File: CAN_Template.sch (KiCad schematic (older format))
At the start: 18 parts

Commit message: Added stack connector and populated PCB
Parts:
- gave numbers to parts that had none: 18
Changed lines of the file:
@@
 EESchema Schematic File Version 4
+LIBS:MASA-Radio Board-cache
 EELAYER 30 0
 EELAYER END
@@
 $EndDescr
 $Comp
-L Device:R_US NP?
+L Device:R_US NP1
 U 1 1 5DCB3E43
 P 6600 3250
-F 0 "NP?" H 6668 3296 50  0000 L CNN
+F 0 "NP1" H 6668 3296 50  0000 L CNN
 F 1 "60" H 6668 3205 50  0000 L CNN
 F 2 "Resistor_SMD:R_0805_2012Metric_Pad1.15x1.40mm_HandSolder" V 6640 3240 50  0001 C CNN
@@
 $EndComp
 $Comp
-L Device:C C?
+L Device:C C3
 U 1 1 5DCB7D7B
 P 4300 2950
-F 0 "C?" V 4048 2950 50  0000 C CNN
+F 0 "C3" V 4048 2950 50  0000 C CNN
 F 1 "100pf" V 4139 2950 50  0000 C CNN
 F 2 "Capacitor_SMD:C_0805_2012Metric_Pad1.15x1.40mm_HandSolder" H 4338 2800 50  0001 C CNN
@@
 $EndComp
 $Comp
-L Device:C C?
+L Device:C C5
 U 1 1 5DCB9CD1
 P 5750 2700
-F 0 "C?" V 5498 2700 50  0000 C CNN
+F 0 "C5" V 5498 2700 50  0000 C CNN
 F 1 "1nf" V 5589 2700 50  0000 C CNN
 F 2 "Capacitor_SMD:C_0805_2012Metric_Pad1.15x1.40mm_HandSolder" H 5788 2550 50  0001 C CNN
@@
 $EndComp
 $Comp
-L Device:C C?
+L Device:C C12
 U 1 1 5DCBAD85
 P 5750 2900
-F 0 "C?" V 5650 2700 50  0000 C CNN
+F 0 "C12" V 5650 2700 50  0000 C CNN
 F 1 "100nf" V 5589 2900 50  0000 C CNN
 F 2 "Capacitor_SMD:C_0805_2012Metric_Pad1.15x1.40mm_HandSolder" H 5788 2750 50  0001 C CNN
@@
 $EndComp
 $Comp
-L power:GND #PWR?
+L power:GND #PWR031
 U 1 1 5DCE500D
 P 3500 3050
-F 0 "#PWR?" H 3500 2800 50  0001 C CNN
+F 0 "#PWR031" H 3500 2800 50  0001 C CNN
 F 1 "GND" H 3505 2877 50  0000 C CNN
 F 2 "" H 3500 3050 50  0001 C CNN
@@
 $EndComp
 $Comp
-L Device:C C?
+L Device:C C14
 U 1 1 5DCE6703
 P 6600 4150
-F 0 "C?" H 6715 4196 50  0000 L CNN
+F 0 "C14" H 6715 4196 50  0000 L CNN
 F 1 "100pf" H 6715 4105 50  0000 L CNN
 F 2 "Capacitor_SMD:C_0805_2012Metric_Pad1.15x1.40mm_HandSolder" H 6638 4000 50  0001 C CNN
@@
 $EndComp
 $Comp
-L Device:R_US NP?
+L Device:R_US NP2
 U 1 1 5DCE98D1
 P 6600 3650
-F 0 "NP?" H 6668 3696 50  0000 L CNN
+F 0 "NP2" H 6668 3696 50  0000 L CNN
 F 1 "60" H 6668 3605 50  0000 L CNN
 F 2 "Resistor_SMD:R_0805_2012Metric_Pad1.15x1.40mm_HandSolder" V 6640 3640 50  0001 C CNN
@@
 $EndComp
 $Comp
-L Device:C C?
+L Device:C C15
 U 1 1 5DCEFDFD
 P 6900 3450
-F 0 "C?" H 7015 3496 50  0000 L CNN
+F 0 "C15" H 7015 3496 50  0000 L CNN
 F 1 "1nf" H 7015 3405 50  0000 L CNN
 F 2 "Capacitor_SMD:C_0805_2012Metric_Pad1.15x1.40mm_HandSolder" H 6938 3300 50  0001 C CNN
@@
 $EndComp
 $Comp
-L power:GND #PWR?
+L power:GND #PWR041
 U 1 1 5DCF0F65
 P 6600 4300
-F 0 "#PWR?" H 6600 4050 50  0001 C CNN
+F 0 "#PWR041" H 6600 4050 50  0001 C CNN
 F 1 "GND" H 6605 4127 50  0000 C CNN
 F 2 "" H 6600 4300 50  0001 C CNN
@@
 $EndComp
 $Comp
-L power:GND #PWR?
+L power:GND #PWR040
 U 1 1 5DCF11EA
 P 6600 2600
-F 0 "#PWR?" H 6600 2350 50  0001 C CNN
+F 0 "#PWR040" H 6600 2350 50  0001 C CNN
 F 1 "GND" H 6605 2427 50  0000 C CNN
 F 2 "" H 6600 2600 50  0001 C CNN
@@
 $EndComp
 $Comp
-L Device:R_US R?
+L Device:R_US R4
 U 1 1 5DCF1CE0
 P 6300 3450
-F 0 "R?" H 6368 3496 50  0000 L CNN
+F 0 "R4" H 6368 3496 50  0000 L CNN
 F 1 "0" H 6368 3405 50  0000 L CNN
 F 2 "Resistor_SMD:R_0805_2012Metric_Pad1.15x1.40mm_HandSolder" V 6340 3440 50  0001 C CNN
@@
 $EndComp
 $Comp
-L Device:D_TVS_x2_CAA D?
+L Device:D_TVS_x2_CAA D2
 U 1 1 5DD0169A
 P 7350 3450
-F 0 "D?" V 7304 3529 50  0000 L CNN
+F 0 "D2" V 7304 3529 50  0000 L CNN
 F 1 "D5V0L2B3W-7" V 7395 3529 50  0000 L CNN
 F 2 "Package_TO_SOT_SMD:SOT-23" H 7200 3450 50  0001 C CNN
@@
 $EndComp
 $Comp
-L Device:R_US R?
+L Device:R_US R3
 U 1 1 5DD5BD7B
 P 4850 3900
-F 0 "R?" H 4918 3946 50  0000 L CNN
+F 0 "R3" H 4918 3946 50  0000 L CNN
 F 1 "10k" H 4918 3855 50  0000 L CNN
 F 2 "Resistor_SMD:R_0805_2012Metric_Pad1.15x1.40mm_HandSolder" V 4890 3890 50  0001 C CNN
@@
 $EndComp
 $Comp
-L Device:R_US R?
+L Device:R_US R2
 U 1 1 5DD67335
 P 4600 3350
-F 0 "R?" H 4668 3396 50  0000 L CNN
+F 0 "R2" H 4668 3396 50  0000 L CNN
 F 1 "0" H 4668 3305 50  0000 L CNN
 F 2 "Resistor_SMD:R_0805_2012Metric_Pad1.15x1.40mm_HandSolder" V 4640 3340 50  0001 C CNN
@@
 $EndComp
 $Comp
-L Interface_CAN_LIN:MCP2515-xSO U?
+L Interface_CAN_LIN:MCP2515-xSO U5
 U 1 1 5DCB05B0
 P 3500 3850
-F 0 "U?" H 3500 3950 50  0000 C CNN
+F 0 "U5" H 3500 3950 50  0000 C CNN
 F 1 "MCP2515-xSO" H 3500 4050 50  0000 C CNN
 F 2 "Package_SO:SOIC-18W_7.5x11.6mm_P1.27mm" H 3500 2950 50  0001 C CIN
@@
 CAN_H
 $Comp
-L Device:C C?
+L Device:C C13
 U 1 1 5DCE5998
 P 6600 2750
-F 0 "C?" H 6715 2796 50  0000 L CNN
+F 0 "C13" H 6715 2796 50  0000 L CNN
 F 1 "100pf" H 6715 2705 50  0000 L CNN
 F 2 "Capacitor_SMD:C_0805_2012Metric_Pad1.15x1.40mm_HandSolder" H 6638 2600 50  0001 C CNN
@@
 $EndComp
 $Comp
-L Interface_CAN_LIN:SN65HVD1050D U?
+L Interface_CAN_LIN:SN65HVD1050D U6
 U 1 1 5DD4ABBA
 P 5450 3450
-F 0 "U?" H 5350 3500 50  0000 C CNN
+F 0 "U6" H 5350 3500 50  0000 C CNN
 F 1 "SN65HVD1050D" H 5350 3400 50  0000 C CNN
 F 2 "Package_SO:SOIC-8_3.9x4.9mm_P1.27mm" H 5450 2950 50  0001 C CNN
@@
 Connection ~ 7350 3000
 $Comp
-L power:GND #PWR?
+L power:GND #PWR037
 U 1 1 5E09CBC9
 P 5450 3850
-F 0 "#PWR?" H 5450 3600 50  0001 C CNN
+F 0 "#PWR037" H 5450 3600 50  0001 C CNN
 F 1 "GND" H 5455 3677 50  0000 C CNN
 F 2 "" H 5450 3850 50  0001 C CNN
@@
 $EndComp
 $Comp
-L power:GND #PWR?
+L power:GND #PWR039
 U 1 1 5E0A1057
 P 5900 2900
-F 0 "#PWR?" H 5900 2650 50  0001 C CNN
+F 0 "#PWR039" H 5900 2650 50  0001 C CNN
 F 1 "GND" H 5905 2727 50  0000 C CNN
 F 2 "" H 5900 2900 50  0001 C CNN
@@
 $EndComp
 $Comp
-L power:GND #PWR?
+L power:GND #PWR038
 U 1 1 5E0A1679
 P 5900 2700
-F 0 "#PWR?" H 5900 2450 50  0001 C CNN
+F 0 "#PWR038" H 5900 2450 50  0001 C CNN
 F 1 "GND" H 5905 2527 50  0000 C CNN
 F 2 "" H 5900 2700 50  0001 C CNN
@@
 Connection ~ 5450 2900
 $Comp
-L power:+5V #PWR?
+L power:+5V #PWR036
 U 1 1 5E0A2EDD
 P 5450 2700
-F 0 "#PWR?" H 5450 2550 50  0001 C CNN
+F 0 "#PWR036" H 5450 2550 50  0001 C CNN
 F 1 "+5V" V 5465 2828 50  0000 L CNN
 F 2 "" H 5450 2700 50  0001 C CNN
@@
 	4850 3650 4950 3650
 $Comp
-L power:GND #PWR?
+L power:GND #PWR035
 U 1 1 5E0A7026
 P 4850 4050
-F 0 "#PWR?" H 4850 3800 50  0001 C CNN
+F 0 "#PWR035" H 4850 3800 50  0001 C CNN
 F 1 "GND" H 4855 3877 50  0000 C CNN
 F 2 "" H 4850 4050 50  0001 C CNN
@@
 $EndComp
 $Comp
-L Device:R_US R?
+L Device:R_US R1
 U 1 1 5E0A7D89
 P 4600 3250
-F 0 "R?" H 4668 3296 50  0000 L CNN
+F 0 "R1" H 4668 3296 50  0000 L CNN
 F 1 "0" H 4668 3205 50  0000 L CNN
 F 2 "Resistor_SMD:R_0805_2012Metric_Pad1.15x1.40mm_HandSolder" V 4640 3240 50  0001 C CNN
@@
 	4750 3350 4850 3350
 $Comp
-L power:GND #PWR?
+L power:GND #PWR033
 U 1 1 5E0B3A8E
 P 4300 2800
-F 0 "#PWR?" H 4300 2550 50  0001 C CNN
+F 0 "#PWR033" H 4300 2550 50  0001 C CNN
 F 1 "GND" H 4305 2627 50  0000 C CNN
 F 2 "" H 4300 2800 50  0001 C CNN
@@
 $EndComp
 $Comp
-L Device:C C?
+L Device:C C2
 U 1 1 5E0BDAE5
 P 3200 5000
-F 0 "C?" V 2948 5000 50  0000 C CNN
+F 0 "C2" V 2948 5000 50  0000 C CNN
 F 1 "1nf" V 3039 5000 50  0000 C CNN
 F 2 "Capacitor_SMD:C_0805_2012Metric_Pad1.15x1.40mm_HandSolder" H 3238 4850 50  0001 C CNN
@@
 $EndComp
 $Comp
-L Device:C C?
+L Device:C C1
 U 1 1 5E0BDAEB
 P 3200 4800
-F 0 "C?" V 3100 4600 50  0000 C CNN
+F 0 "C1" V 3100 4600 50  0000 C CNN
 F 1 "100nf" V 3039 4800 50  0000 C CNN
 F 2 "Capacitor_SMD:C_0805_2012Metric_Pad1.15x1.40mm_HandSolder" H 3238 4650 50  0001 C CNN
@@
 $EndComp
 $Comp
-L power:GND #PWR?
+L power:GND #PWR029
 U 1 1 5E0BDAF1
 P 3050 4800
-F 0 "#PWR?" H 3050 4550 50  0001 C CNN
+F 0 "#PWR029" H 3050 4550 50  0001 C CNN
 F 1 "GND" H 3055 4627 50  0000 C CNN
 F 2 "" H 3050 4800 50  0001 C CNN
@@
 $EndComp
 $Comp
-L power:GND #PWR?
+L power:GND #PWR030
 U 1 1 5E0BDAF7
 P 3050 5000
-F 0 "#PWR?" H 3050 4750 50  0001 C CNN
+F 0 "#PWR030" H 3050 4750 50  0001 C CNN
 F 1 "GND" H 3055 4827 50  0000 C CNN
 F 2 "" H 3050 5000 50  0001 C CNN
@@
 Connection ~ 3500 4800
 $Comp
-L power:+5V #PWR?
+L power:+5V #PWR032
 U 1 1 5E0BDB02
 P 3500 5000
-F 0 "#PWR?" H 3500 4850 50  0001 C CNN
+F 0 "#PWR032" H 3500 4850 50  0001 C CNN
 F 1 "+5V" V 3515 5128 50  0000 L CNN
 F 2 "" H 3500 5000 50  0001 C CNN
@@
 Connection ~ 3500 5000
 $Comp
-L Device:C C?
+L Device:C C4
 U 1 1 5E0C191D
 P 4450 3600
-F 0 "C?" V 4600 3600 50  0000 C CNN
+F 0 "C4" V 4600 3600 50  0000 C CNN
 F 1 "100pf" V 4289 3600 50  0000 C CNN
 F 2 "Capacitor_SMD:C_0805_2012Metric_Pad1.15x1.40mm_HandSolder" H 4488 3450 50  0001 C CNN
@@
 $EndComp
 $Comp
-L power:GND #PWR?
+L power:GND #PWR034
 U 1 1 5E0C3AF0
 P 4300 3600
-F 0 "#PWR?" H 4300 3350 50  0001 C CNN
+F 0 "#PWR034" H 4300 3350 50  0001 C CNN
 F 1 "GND" H 4305 3427 50  0000 C CNN
 F 2 "" H 4300 3600 50  0001 C CNN
@@
 	7050 3450 7100 3450
 $Comp
-L power:GND #PWR?
+L power:GND #PWR042
 U 1 1 5E0C862A
 P 7100 3450
-F 0 "#PWR?" H 7100 3200 50  0001 C CNN
+F 0 "#PWR042" H 7100 3200 50  0001 C CNN
 F 1 "GND" H 7105 3277 50  0000 C CNN
 F 2 "" H 7100 3450 50  0001 C CNN

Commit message: Modified CAN from 5.0V to 3.3V
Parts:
- added C95: 100pF, symbol Device:C_Small
- added U91, U92: SN74LVC1T45DBVR, digikey-footprints:SOT-23-6, symbol dk_Logic-Translators-Level-Shifters:SN74LVC1T45DBVR
- renumbered C1 to C91, C14 to C910, C2 to C92, C3 to C93, C4 to C94, C5 to C96, C12 to C97, C13 to C98, C15 to C99, D2 to D92, R1 to R91, R2 to R92, R3 to R95, R4 to R96
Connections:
- net GND: now also C95.1, U91.2 (GND), U92.2 (GND), U92.5 (DIR)
- net at C94.2, R92.1: now also U91.3 (A); no longer U6.1 (TXD)
- net at U6.4 (RXD): now also U92.4 (B); no longer R91.2
- new net: C95.2, U6.1 (TXD), U91.4 (B)
- new net: R91.2, U92.3 (A)
- new net +3V3: U91.5 (DIR)
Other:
- moved on the sheet: C91, C910, C92, C93, C94, C96, C97, C98, C99, D92, NP1, NP2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

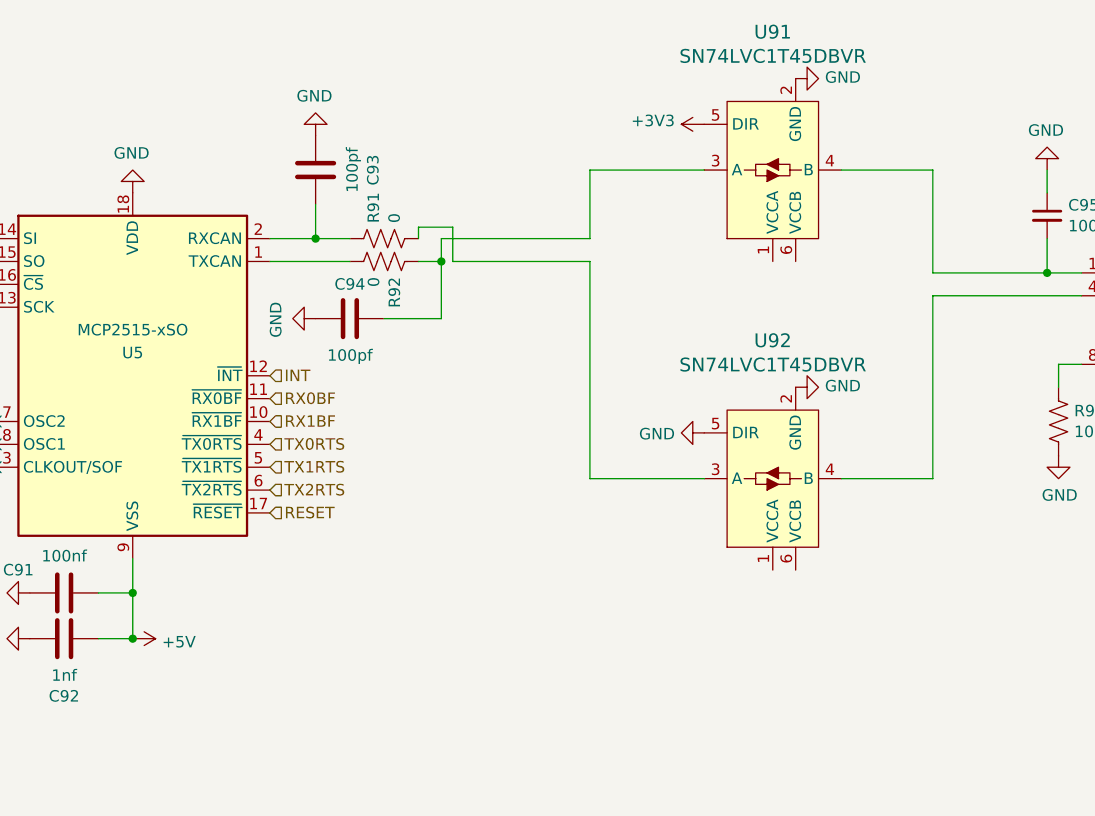
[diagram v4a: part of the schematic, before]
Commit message: fixed/added values
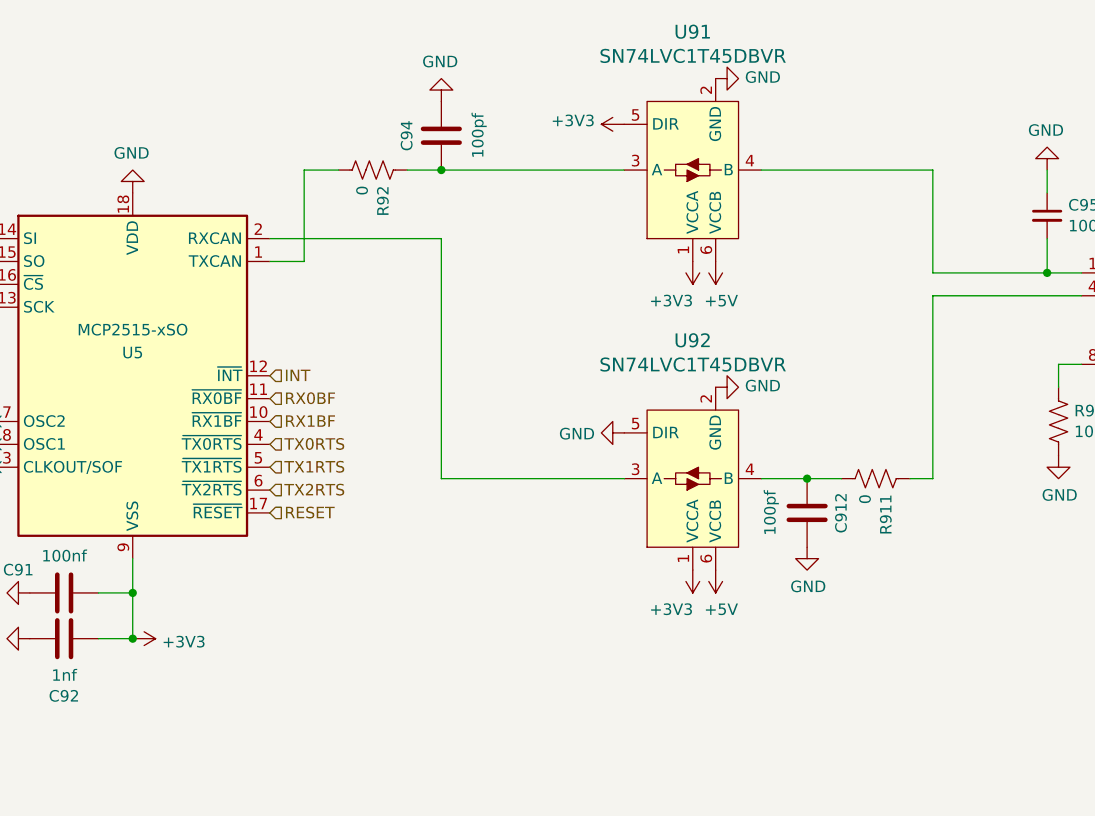
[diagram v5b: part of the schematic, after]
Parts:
- removed C93: 100pf, Capacitor_SMD:C_0805_2012Metric_Pad1.15x1.40mm_HandSolder, symbol Device:C
- removed R91: 0, Resistor_SMD:R_0805_2012Metric_Pad1.15x1.40mm_HandSolder, symbol Device:R_US
- added C912: 100pf, Capacitor_SMD:C_0805_2012Metric_Pad1.15x1.40mm_HandSolder, symbol Device:C
- added R911: 0, Resistor_SMD:R_0805_2012Metric_Pad1.15x1.40mm_HandSolder, symbol Device:R_US
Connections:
- net +3V3: now also C91.1, C92.2, U5.9 (VSS), U91.1 (VCCA), U92.1 (VCCA)
- net +5V: now also U91.6 (VCCB), U92.6 (VCCB); no longer C91.1, C92.2, U5.9 (VSS)
- net GND: now also C94.2, C912.2; no longer C94.1
- net at U5.2 (RXCAN): now also U92.3 (A)
- net at U6.4 (RXD): now also R911.1; no longer U92.4 (B)
- net at R92.1, U91.3 (A): now also C94.1; no longer C94.2
- new net: C912.1, R911.2, U92.4 (B)
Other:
- moved on the sheet: C94, R92, U91, U92

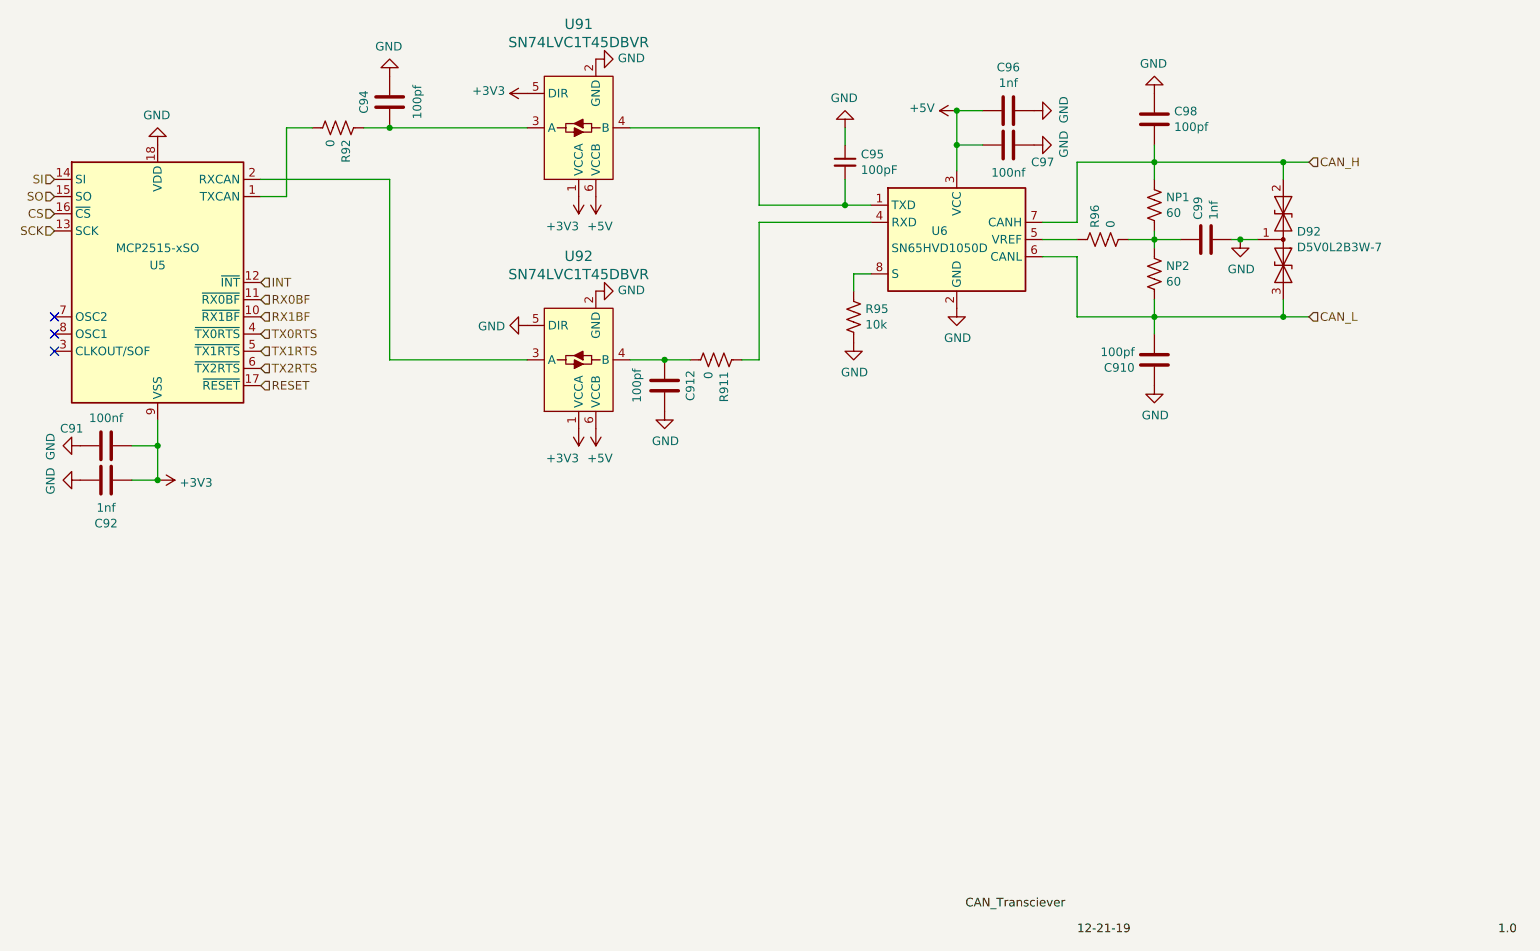
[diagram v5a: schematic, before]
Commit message: Some minor footprint and value updates - unfinished
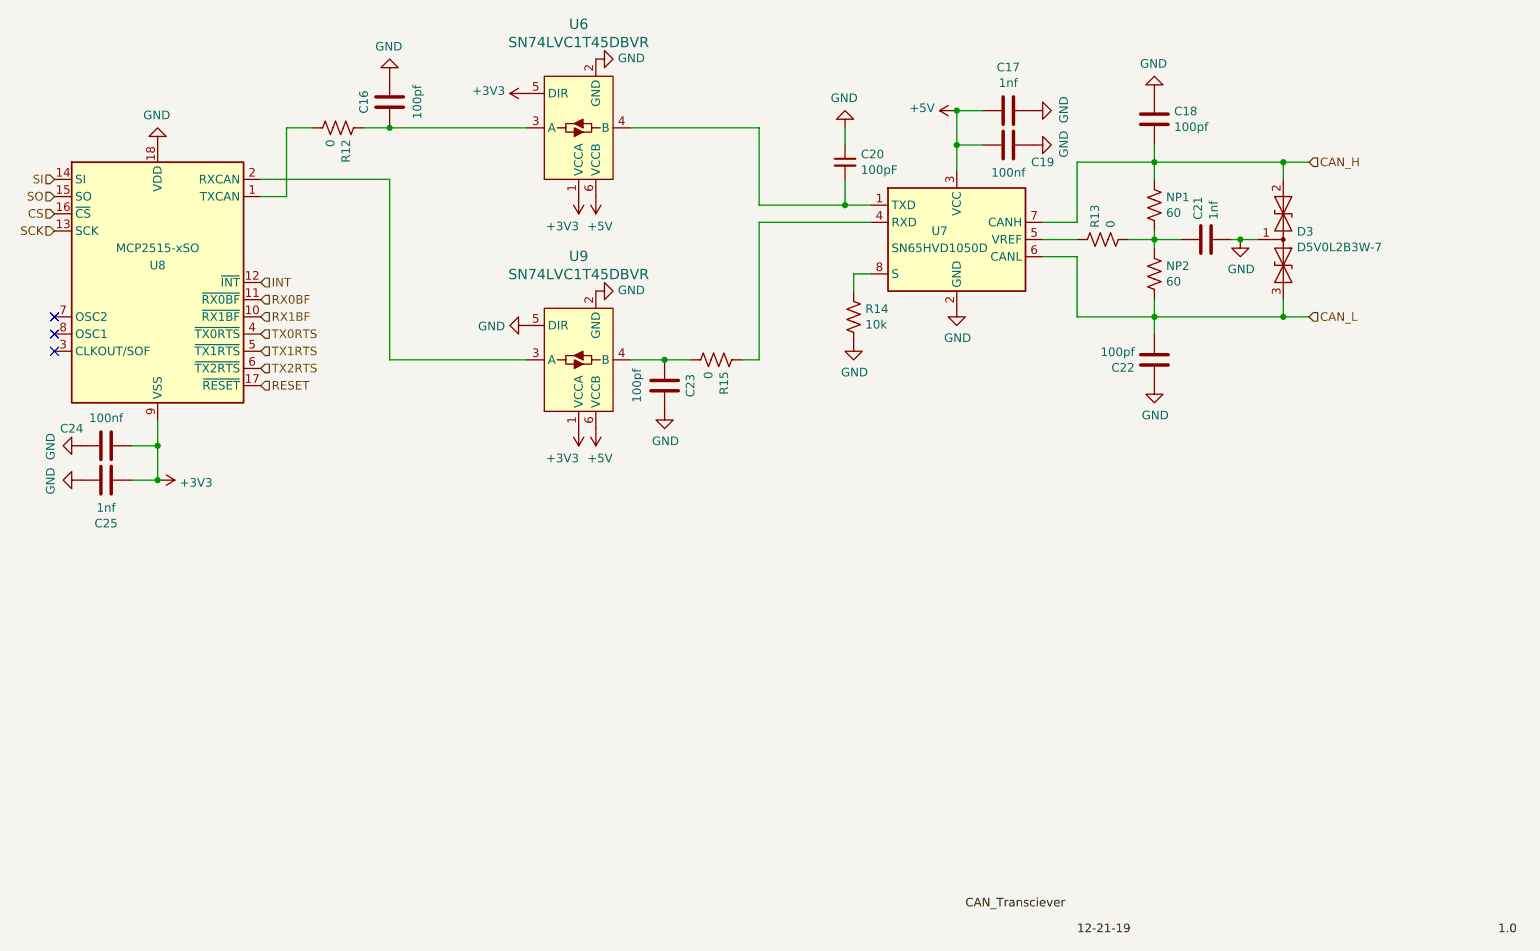
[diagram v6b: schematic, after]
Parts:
- C16: renamed from C94; footprint Capacitor_SMD:C_0805_2012Metric_Pad1.15x1.40mm_HandSolder -> Capacitor_SMD:C_0805_2012Metric
- C17: renamed from C96; footprint Capacitor_SMD:C_0805_2012Metric_Pad1.15x1.40mm_HandSolder -> Capacitor_SMD:C_0805_2012Metric
- C18: renamed from C98; footprint Capacitor_SMD:C_0805_2012Metric_Pad1.15x1.40mm_HandSolder -> Capacitor_SMD:C_0805_2012Metric
- C19: renamed from C97; footprint Capacitor_SMD:C_0805_2012Metric_Pad1.15x1.40mm_HandSolder -> Capacitor_SMD:C_0805_2012Metric
- C20: renamed from C95; footprint (none) -> Capacitor_SMD:C_0805_2012Metric
- C21: renamed from C99; footprint Capacitor_SMD:C_0805_2012Metric_Pad1.15x1.40mm_HandSolder -> Capacitor_SMD:C_0805_2012Metric
- C22: renamed from C910; footprint Capacitor_SMD:C_0805_2012Metric_Pad1.15x1.40mm_HandSolder -> Capacitor_SMD:C_0805_2012Metric
- C23: renamed from C912; footprint Capacitor_SMD:C_0805_2012Metric_Pad1.15x1.40mm_HandSolder -> Capacitor_SMD:C_0805_2012Metric
- C24: renamed from C91; footprint Capacitor_SMD:C_0805_2012Metric_Pad1.15x1.40mm_HandSolder -> Capacitor_SMD:C_0805_2012Metric
- C25: renamed from C92; footprint Capacitor_SMD:C_0805_2012Metric_Pad1.15x1.40mm_HandSolder -> Capacitor_SMD:C_0805_2012Metric
- NP1, NP2: footprint Resistor_SMD:R_0805_2012Metric_Pad1.15x1.40mm_HandSolder -> Resistor_SMD:R_0805_2012Metric
- R12: renamed from R92; footprint Resistor_SMD:R_0805_2012Metric_Pad1.15x1.40mm_HandSolder -> Resistor_SMD:R_0805_2012Metric
- R13: renamed from R96; footprint Resistor_SMD:R_0805_2012Metric_Pad1.15x1.40mm_HandSolder -> Resistor_SMD:R_0805_2012Metric
- R14: renamed from R95; footprint Resistor_SMD:R_0805_2012Metric_Pad1.15x1.40mm_HandSolder -> Resistor_SMD:R_0805_2012Metric
- R15: renamed from R911; footprint Resistor_SMD:R_0805_2012Metric_Pad1.15x1.40mm_HandSolder -> Resistor_SMD:R_0805_2012Metric
- renumbered D92 to D3, U91 to U6, U6 to U7, U5 to U8, U92 to U9
